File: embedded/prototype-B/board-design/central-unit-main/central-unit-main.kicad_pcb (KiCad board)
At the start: 2 copper layers, 45 x 92.5 mm, 100 parts, among them IC2 VEML6030, IC3 STM1061N27WX6F, J1 Screw_Terminal_01x02, J2 2171790001, J3 Conn_02x05_Odd_Even, J4 Conn_02x05_Odd_Even, J5 Conn_ARM_JTAG_SWD_20, SW1 CAS-120TA1, U1 STM32L452RETx, U2 TPS63000, U3 BQ24074RGT, U4 USBLC6-2SC6, U5 LIS2HH12, Y1 ECS-_327-12_5-34B-TR, Y2 STDCSU1-8M

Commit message: [All] Schematic review
Fixed load capacitor values for the oscillators.

Signed-off-by: Nicolae-Andrei Prodan <vasilenicolaeandrei@gmail.com>
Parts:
- C13, C14: value 100nF/6.3V/20%/C0603 -> 18pF/6.3V/20%/C0603
- C15, C16: value 100nF/6.3V/20%/C0603 -> 10pF/6.3V/20%/C0603
- renumbered D3 to D2, D4 to D3, FB4 to FB1, FB3 to FB2, IC3 to IC1, J5 to J4, J4 to J5, R14 to R13, R13 to R14, S2 to S1, U4 to U3, U3 to U4

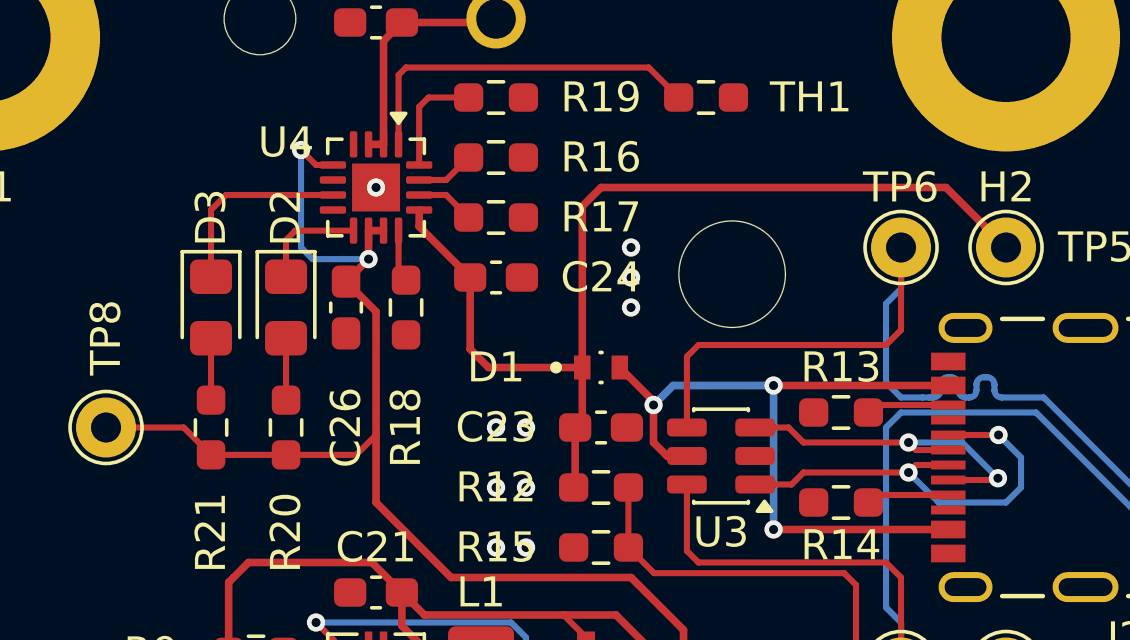
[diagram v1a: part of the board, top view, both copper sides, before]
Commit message: [Central unit] Fix ESD protection circuit for USB connector
Removed series diode from the USB connector design.

Signed-off-by: Nicolae-Andrei Prodan <vasilenicolaeandrei@gmail.com>
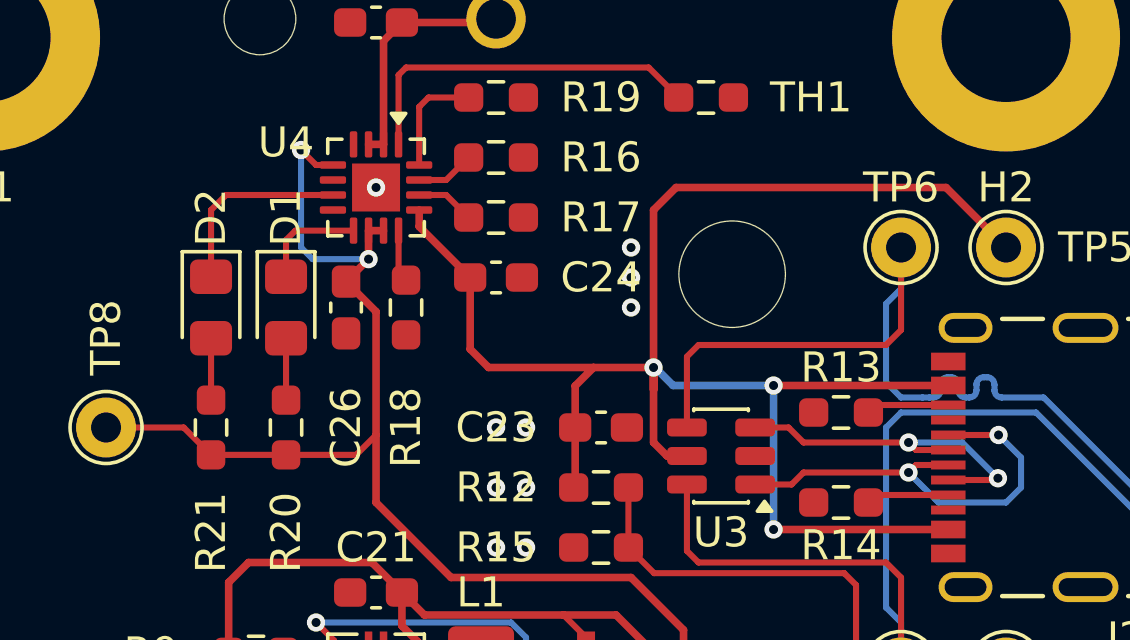
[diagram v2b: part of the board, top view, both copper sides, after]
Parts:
- removed the D1 at (145.5, 65.0)
- renumbered D2 to D1, D3 to D2
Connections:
- J2 pad A4B9: Net-(J2-VBUS1) -> VBUS
- J2 pad B4A9: Net-(J2-VBUS1) -> VBUS
- U3 pad 5: Net-(J2-VBUS1) -> VBUS
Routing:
- net VBUS: track 34.0 -> 60.9 mm, vias 0 -> 3
- net Net-(J2-VBUS1): track 25.4 -> 0.00 mm, vias 3 -> 0

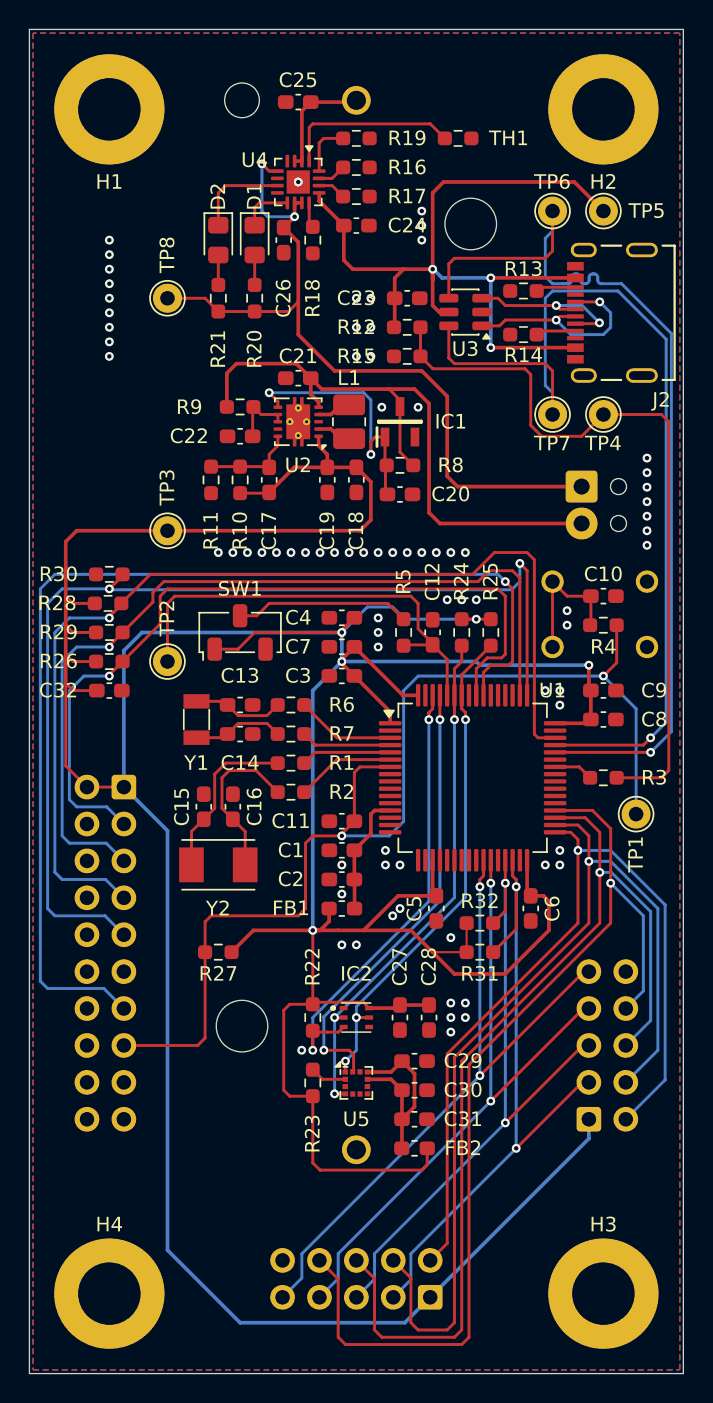
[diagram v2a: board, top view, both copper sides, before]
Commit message: [Central unit] Redesign voltage supervisor
Refactored voltage supervisor for the converter. Added the diode for the
VBUS back.

Signed-off-by: Nicolae-Andrei Prodan <vasilenicolaeandrei@gmail.com>
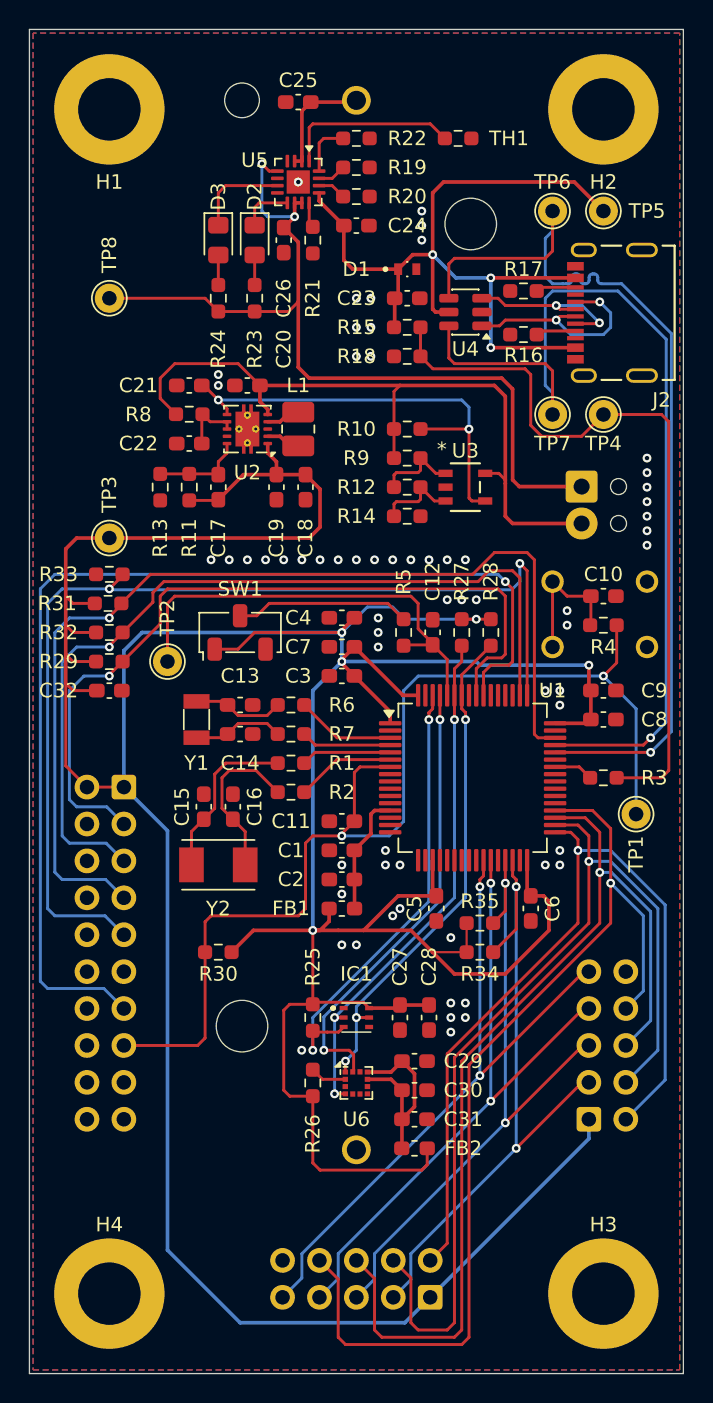
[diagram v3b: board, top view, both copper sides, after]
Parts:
- removed the IC1 at (145.0, 75.5)
- removed the R8 at (145.0, 78.5)
- added D1: ESDA7P60-1U1M, ESDA7P60-1U1M:TVS_ESDA7P60-1U1M, F.Cu at (145.5, 65.0)
- added R10: 100K/R0603, Resistor_SMD:R_0603_1608Metric_Pad0.98x0.95mm_HandSolder, F.Cu at (145.5, 76.0)
- added R12: 56K/R0603, Resistor_SMD:R_0603_1608Metric_Pad0.98x0.95mm_HandSolder, F.Cu at (145.5, 80.0)
- added R14: 340K/R0603, Resistor_SMD:R_0603_1608Metric_Pad0.98x0.95mm_HandSolder, F.Cu at (145.5, 82.0)
- added R9: 604K/R0603, Resistor_SMD:R_0603_1608Metric_Pad0.98x0.95mm_HandSolder, F.Cu at (145.5, 78.0)
- added U3: MIC2778-2YM5-TR, MIC2778:MIC2778, F.Cu at (149.5, 80.0)
- moved C21 16.3 mm to (130.5, 73.0), turned to 180 degrees
- moved TP3 4.03 mm to (125.0, 83.5)
- moved TP8 4.00 mm to (125.0, 67.0)
- moved C17 3.54 mm to (132.5, 80.0)
- moved C18 3.54 mm to (138.5, 80.0)
- moved C19 3.54 mm to (136.5, 80.0)
- moved C20 3.54 mm to (134.5, 73.0)
- moved C22 3.54 mm to (130.5, 77.0)
- moved L1 3.54 mm to (138.0, 76.0)
- moved R11 3.54 mm to (130.5, 80.0)
- moved R13 3.54 mm to (128.5, 80.0)
- moved R8 3.54 mm to (130.5, 75.0)
- moved U2 3.54 mm to (134.5, 76.0)
- renumbered C21 to C20, C20 to C21, D1 to D2, D2 to D3, IC2 to IC1, R10 to R11, R11 to R13, R12 to R15, R14 to R16, R13 to R17, R15 to R18, R16 to R19, R17 to R20, R18 to R21, R19 to R22, R20 to R23, R21 to R24, R22 to R25, R23 to R26, R24 to R27, R25 to R28, R26 to R29, R27 to R30, R28 to R31, R29 to R32, R30 to R33, R31 to R34, R32 to R35, R9 to R8, U3 to U4, U4 to U5, U5 to U6
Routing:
- net Net-(U2-EN): track 18.3 -> 31.0 mm
- net Net-(J1-Pin_2): track 44.1 -> 50.7 mm
- net Net-(U3-HTH): track 0.00 -> 5.79 mm
- net +BATT: track 53.9 -> 59.7 mm
- net Net-(U3-LTH): track 0.00 -> 5.75 mm
- net +3V3: track 325.4 -> 321.4 mm
- net VBUS: track 60.9 -> 59.9 mm
- net GND: vias 76 -> 64

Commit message: [Central unit] Change the battery charging configuration
Changed battery charger configuration to USB500. Moved voltage monitor
threshold voltage divider and power supply upstream of J1 as well.

Signed-off-by: Nicolae-Andrei Prodan <vasilenicolaeandrei@gmail.com>
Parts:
- removed the R19 at (142.0, 58.0)
- added C20: 10uF/6.3V/20%/C0603, Capacitor_SMD:C_0603_1608Metric_Pad1.08x0.95mm_HandSolder, F.Cu at (153.4, 82.0)
- R19: renamed from R20; value 46.4K/R0603 -> 68K/R0603
- R20: renamed from R21; value 1.18K/R0603 -> 3.48K/R0603
- R21: renamed from R22; value 1.13K/R0603 -> 2.21K/R0603
- TH1: value 10K/TH0603 -> 10K/TH0603 (NTC)
- moved TH1 7.00 mm to (142.0, 56.0)
- moved R21 2.00 mm to (142.0, 58.0)
- renumbered C20 to C21, C21 to C22, C22 to C23, C23 to C24, C24 to C25, C25 to C26, C26 to C27, C27 to C28, C28 to C29, C29 to C30, C30 to C31, C31 to C32, C32 to C33, R23 to R22, R24 to R23, R25 to R24, R26 to R25, R27 to R26, R28 to R27, R29 to R28, R30 to R29, R31 to R30, R32 to R31, R33 to R32, R34 to R33, R35 to R34
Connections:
- R9 pad 1: Net-(J1-Pin_2) -> +BATT
- U3 pad 5: Net-(J1-Pin_2) -> +BATT
- U5 pad 15: Net-(U5-ITERM) -> unconnected-(U5-ITERM-Pad15)
- U5 pad 5: +BATT -> GND
- U5 pad 6: GND -> +BATT
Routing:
- net +BATT: track 59.7 -> 73.2 mm, vias 2 -> 4
- net Net-(U5-TS): track 12.2 -> 3.61 mm
- net Net-(U5-ISET): track 3.72 -> 1.75 mm
- net Net-(U5-ITERM): track 1.96 -> 0.00 mm
- net Net-(J1-Pin_2): track 50.7 -> 50.2 mm
- net GND: vias 64 -> 70

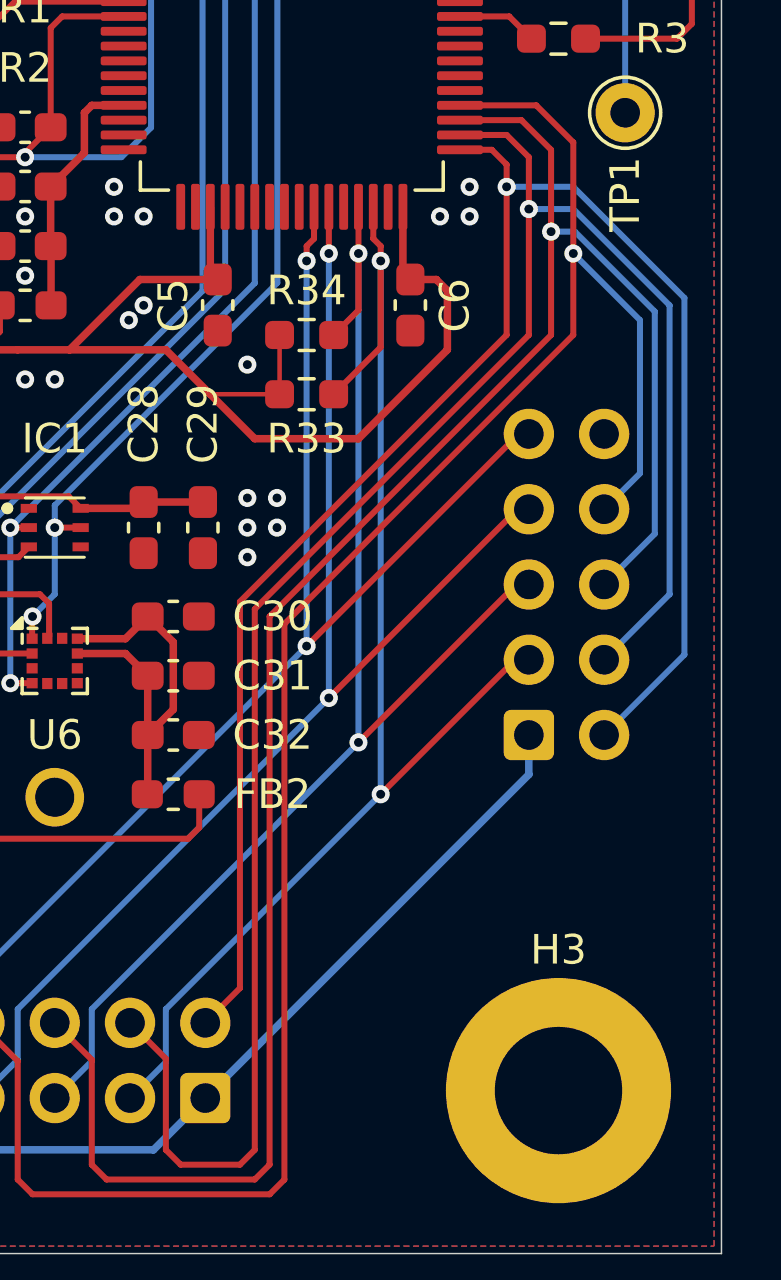
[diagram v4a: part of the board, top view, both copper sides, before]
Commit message: [Light] Led driver reset pin enhacement
Removed the second pinhead for the lighting PCB. Only one can connect to
the main board as of now.

Signed-off-by: Nicolae-Andrei Prodan <vasilenicolaeandrei@gmail.com>
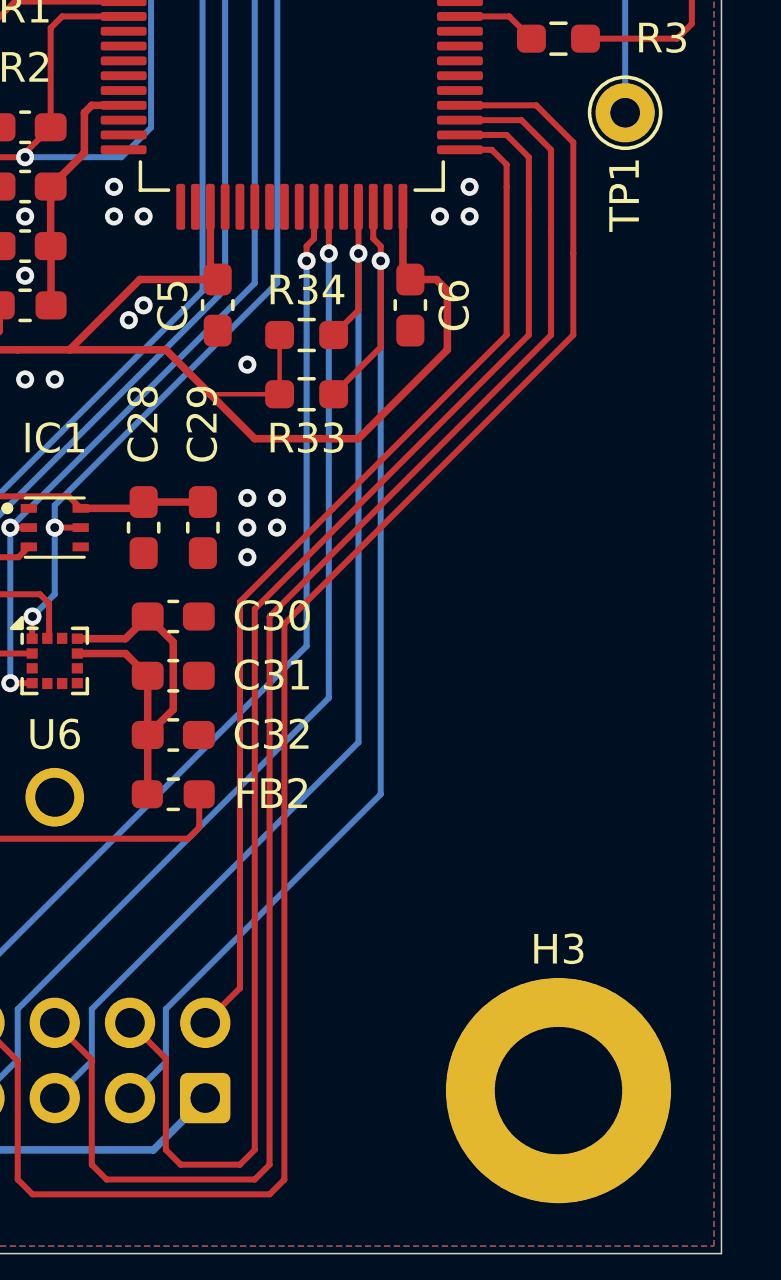
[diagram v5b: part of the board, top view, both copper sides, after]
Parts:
- removed J5: Conn_02x05_Odd_Even, Connector_IDC:IDC-Header_2x05_P2.54mm_Vertical
- R33, R34: value 10K/R0603 -> 4.7K/R0603
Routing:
- net /Connector/SPI_SS: track 58.4 -> 35.0 mm, vias 1 -> 0
- net /Connector/SPI_SCK: track 67.1 -> 48.2 mm, vias 1 -> 0
- net +3V3: track 321.4 -> 304.6 mm
- net /Connector/SPI_MISO: track 67.9 -> 53.4 mm, vias 1 -> 0
- net /Connector/GPIO0: track 46.3 -> 35.8 mm, vias 2 -> 1
- net /Connector/SPI_MOSI: track 68.7 -> 58.6 mm, vias 1 -> 0
- net /Connector/GPIO1: track 44.3 -> 35.0 mm, vias 2 -> 1
- net /Connector/I2C_SCL: track 45.4 -> 37.4 mm, vias 2 -> 1
- net /Connector/I2C_SDA: track 45.7 -> 38.8 mm, vias 2 -> 1

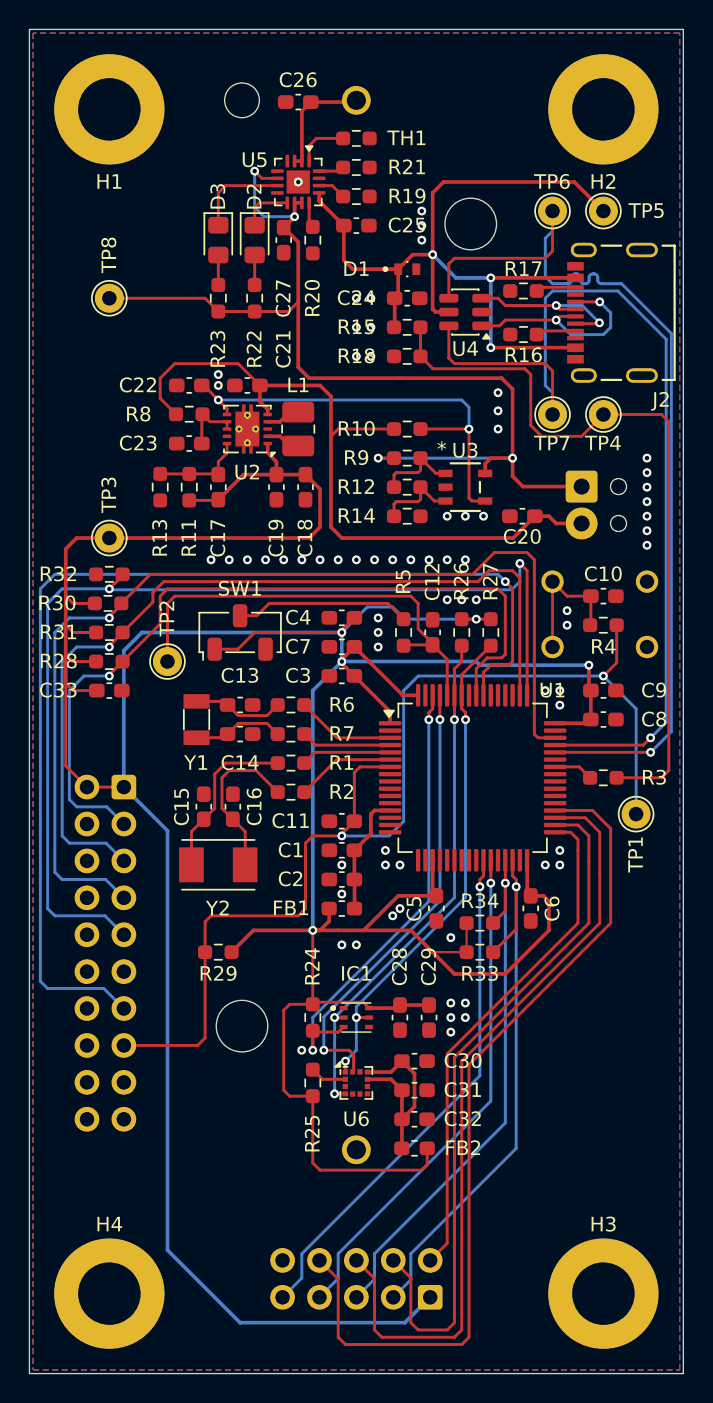
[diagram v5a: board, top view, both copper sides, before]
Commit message: [Central unit] Improve BQ24074 layout
Refactored the entire PCB layout.

Signed-off-by: Nicolae-Andrei Prodan <vasilenicolaeandrei@gmail.com>
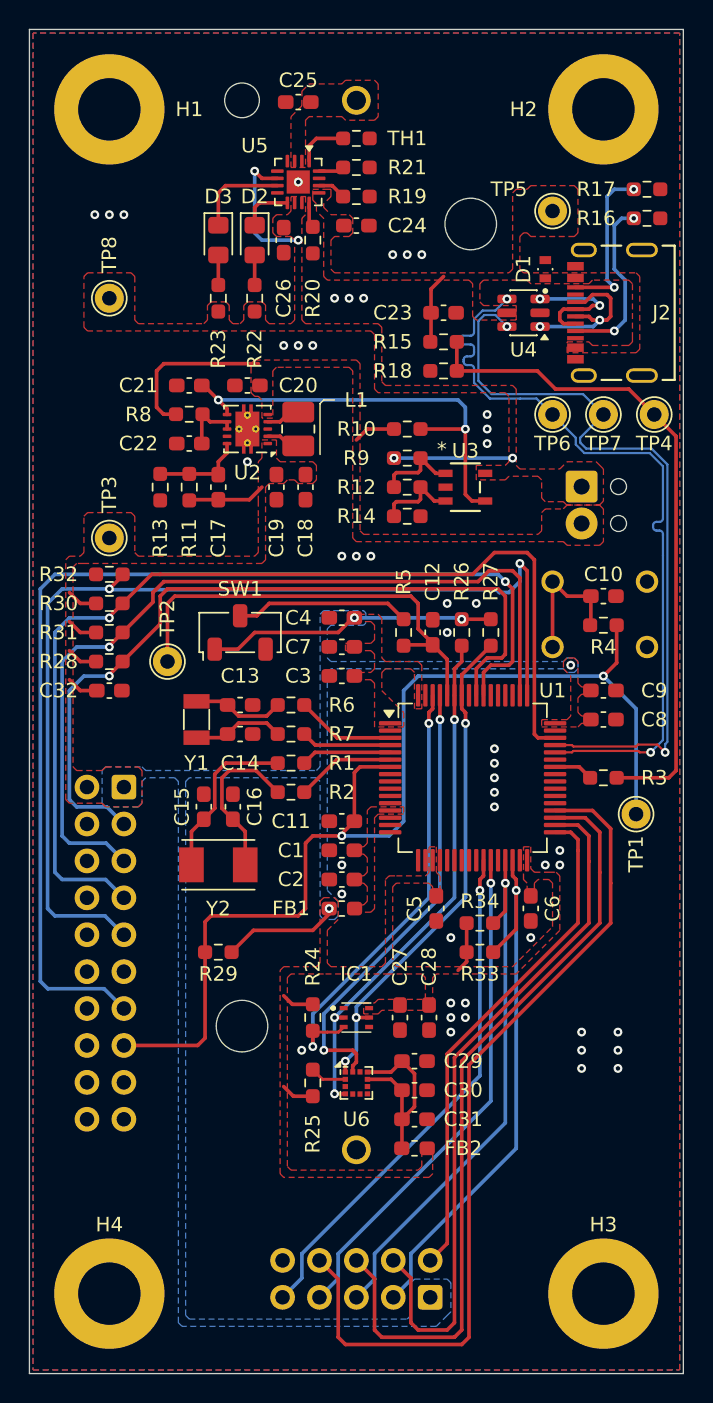
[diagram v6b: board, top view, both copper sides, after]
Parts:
- removed the C20 at (153.4, 82.0)
- moved TP6 14.0 mm to (155.5, 75.0), turned to 180 degrees
- moved R16 11.7 mm to (162.0, 61.5), turned to 0 degrees
- moved R17 11.0 mm to (162.0, 59.5), turned to 0 degrees
- moved D1 9.50 mm to (155.0, 65.0), turned to 90 degrees
- moved U4 4.00 mm to (153.5, 68.0)
- moved TP4 3.50 mm to (162.5, 75.0)
- moved TP5 3.50 mm to (155.5, 61.0)
- moved TP7 3.50 mm to (159.0, 75.0)
- moved C23 2.69 mm to (148.0, 68.0)
- moved R15 2.69 mm to (148.0, 70.0)
- moved R18 2.69 mm to (148.0, 72.0)
- moved R30 0.09 mm to (125.0, 88.0)
- renumbered C21 to C20, C22 to C21, C23 to C22, C24 to C23, C25 to C24, C26 to C25, C27 to C26, C28 to C27, C29 to C28, C30 to C29, C31 to C30, C32 to C31, C33 to C32
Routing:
- net +3V3: track 304.6 -> 50.1 mm, vias 5 -> 4
- net +BATT: track 73.2 -> 17.4 mm
- net VBUS: track 59.9 -> 4.88 mm, vias 3 -> 0
- net Net-(J1-Pin_2): track 50.2 -> 14.1 mm
- net /MCU/USB_D-: track 65.4 -> 53.0 mm, vias 1 -> 2
- net /MCU/USB_D+: track 65.5 -> 53.1 mm, vias 1 -> 2
- net Net-(J2-CC1): track 2.77 -> 12.1 mm, vias 0 -> 2
- net Net-(J2-CC2): track 2.77 -> 11.2 mm, vias 0 -> 2
- net /MCU/VDDA: track 8.40 -> 0.00 mm
- net Net-(BAT1-+): track 8.00 -> 0.00 mm
- net /MCU/USB_DETECT: track 52.0 -> 46.2 mm
- net Net-(J2-DP1): track 14.8 -> 10.9 mm
- net Net-(J2-DN1): track 11.9 -> 8.93 mm
- net /MCU/ALS_INT: track 31.5 -> 31.0 mm
- net GND: vias 70 -> 47
- added copper zone on B.Cu, net +3V3
- added copper zone on F.Cu, net +3V3
- added copper zone on F.Cu, net +BATT
- added copper zone on F.Cu, net /MCU/VDDA
- added copper zone on F.Cu, net Net-(BAT1-+)
- added copper zone on F.Cu, net Net-(J1-Pin_2)
- added copper zone on F.Cu, net VBUS
